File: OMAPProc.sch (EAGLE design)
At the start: 11 parts

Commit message: Pre-reinstall commit
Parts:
- removed C30, C31, C32, C33: 0.1uF, SparkFun:CAP0402-CAP
- removed JP11: MPCS6PH, stan:MPCS6PH
- removed R18: 4.7k, rcl:R-US_R0402
- removed R19, R20: 1.5k, rcl:R-US_R0402
- removed SHIFT1: TXS0108E, user:TXS0108E
- added C1, C15, C16, C17, C18, C19, C2, C21, C22, C3, C8: 0.1uF, biomimetic:CAP0402-CAP
- added C10, C11, C12, C13, C14, C4, C5, C6, C9: 1uF, biomimetic:CAP0402-CAP
- added C20: (no value), biomimetic:CAP0603-CAP
- added C7: 22uF, biomimetic:CAP0603-CAP
- added CAM2: ECAM50_5642_MOD, biomimetic:ECAM50_5642_MOD
- added IC1: MIC5335-SPYMT, biomimetic:MIC5335-SPYMT
- added IC2: MIC5335-MGYMT, biomimetic:MIC5335-MGYMT
- added IC3: TXS0108ERGY, biomimetic:TXS0108ERGY
- added JP1: Console, biomimetic:MOLEX_503480-0600
- added JP2: ImageProc, biomimetic:MOLEX_503480-0600
- added R1, R2: 1.5k, biomimetic:RESISTOR0402-RES
- added R3, R4, R5, R6, R7: 10k, biomimetic:RESISTOR0402-RES
- added R8: DNP, biomimetic:RESISTOR0402-RES
- added S1: SW_RESET, SparkFun-Electromechanical:SWITCH-MOMENTARY-2-SMD-1101NE
- added S2: SW_PWRON, SparkFun-Electromechanical:SWITCH-MOMENTARY-2-SMD-1101NE
- added SDCARD1: MICROSD, biomimetic:MICROSD
- CAM1: value AXK7L28227G(LI-VM01CM) -> LI-VM01CM; device user:AXK7L28227G(LI-VM01CM) -> biomimetic:LI-VM01CM
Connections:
- removed net N$18: SHIFT1.B1
- removed net N$22: SHIFT1.B2
- removed net N$27: SHIFT1.B3
- removed net N$30: SHIFT1.B4
- removed net N$31: SHIFT1.B5
- removed net N$33: SHIFT1.B6
- removed net N$34: SHIFT1.B7
- removed net N$35: SHIFT1.B8
- removed net OMAP_1.8V: C30.1, C32.1, CAM1.DOVDD(2.8V), CAM1.DVDD(1.8V), R18.2, R19.2, R20.2, SHIFT1.OE, SHIFT1.VCCA
- removed net OMAP_3.0V: C31.2, CAM1.AVDD(2.8V)
- removed net OMAP_3.3V: C33.1, SHIFT1.VCCB
- removed net OMAP_GND: C30.2, C31.1, C32.2, C33.2, CAM1.AGND, CAM1.DGND, JP11.2, R18.1, SHIFT1.GND
- removed net OMAP_SPI2_CLK: SHIFT1.A1
- removed net OMAP_SPI2_CS0: SHIFT1.A4
- removed net OMAP_SPI2_CS1: SHIFT1.A5
- removed net OMAP_SPI2_IRQ: SHIFT1.A6
- removed net OMAP_SPI2_SIMO: SHIFT1.A2
- removed net OMAP_SPI2_SOMI: SHIFT1.A3
- removed net OMAP_SPI4_CLK: SHIFT1.A7
- removed net OMAP_SPI4_SIMO: SHIFT1.A8
- removed net TERMINAL_CTS: JP11.6
- removed net TERMINAL_RTS: JP11.5
- removed net TERMINAL_RX: JP11.3
- removed net TERMINAL_TX: JP11.4
- new net !RESET: CAM1_S.!RESET, CAM2_S.!RESET, SOM1_CLOCKRESET.SYS_NRESWARM
- new net 1.8V: C1.2, C11.1, C15.1, C19.1, C2.1, C4.1, C5.2, CAM1_DOVDD.V+, CAM1_DVDD.V+, CAM2_DOVDD.V+, IC2.1.8V, IC3.OE, IC3.VCCA, R1.1, R2.1
- new net 2.8V: C10.1, C18.1, C3.1, C6.1, CAM1_AVDD.V+, CAM2_AVDD.V+, IC2.2.8V
- new net 3.0V: C14.1, IC1.3.0
- new net 3.3V: C13.1, C16.1, C17.1, CAM2_AFVCC.V+, IC1.3.3V, IC3.VCCB
- new net GND: C1.1, C10.2, C11.2, C12.1, C13.2, C14.2, C15.2, C16.2, C17.2, C18.2, C19.2, C2.2, C20.2, C21.2, C22.2, C3.2, C4.2, C5.1, C6.2, C7.2, C8.2, C9.1, CAM1_AGND.V-, CAM1_DGND.V-, CAM1_S.STANDBY, CAM2_AFVCC.V-, CAM2_AVDD.V-, CAM2_DOVDD.V-, CAM2_S.PWDN, IC1.GND, IC2.GND, IC3.GND, JP1.1, JP2.3, JP2.5, SDCARD1.CASE, SDCARD1.COM, SDCARD1.VSS, SOM1_DGND.V-
- new net MSTR_NRST: C21.1, S1.1, SOM1_CLOCKRESET.MSTR_NRST
- new net N$3: S1.2, S2.2
- new net PWRON: C22.1, S2.1, SOM1_CLOCKRESET.PWRON
- new net SD1_CD: R8.1, SDCARD1.CD, SOM1_GPIO.UP_GPIO_127
- new net SD1_CLK: SDCARD1.CLK, SOM1_SDMMC.SD1_CLK
- new net SD1_CMD: R3.1, SDCARD1.CMD, SOM1_SDMMC.SD1_CMD
- new net SD1_DATA0: R4.1, SDCARD1.DAT0, SOM1_SDMMC.SD1_DATA0
- new net SD1_DATA1: R5.1, SDCARD1.DAT1, SOM1_SDMMC.SD1_DATA1
- new net SD1_DATA2: R6.1, SDCARD1.DAT2, SOM1_SDMMC.SD1_DATA2
- new net SD1_DATA3: R7.1, SDCARD1.DAT3/CD, SOM1_SDMMC.SD1_DATA3
- new net UARTA_CTS: JP1.6, SOM1_UART.UP_UARTA_CTS
- new net UARTA_RTS: JP1.2, SOM1_UART.UP_UARTA_RTS
- new net UARTA_RX: JP1.4, SOM1_UART.UP_UARTA_RX
- new net UARTA_TX: JP1.5, SOM1_UART.UP_UARTA_TX
- new net UARTB_RX: IC3.A2, SOM1_UART.UP_UARTB_RX
- new net UARTB_RX_3V3: IC3.B2, JP2.4
- new net UARTB_TX: IC3.A1, SOM1_UART.UP_UARTB_TX
- new net UARTB_TX_3V3: IC3.B1, JP2.6
- new net VMMC1: C7.1, C8.1, R3.2, R4.2, R5.2, R6.2, R7.2, R8.2, SDCARD1.VDD, SOM1_SDMMC.VMMC1
- new net V_BATT: C12.2, C20.1, C9.2, IC1.EN_3.0V, IC1.EN_3.3V, IC1.VIN, IC2.EN_1.8V, IC2.EN_2.8V, IC2.VIN, JP2.1, JP2.2, SOM1_MAIN_BATTERY.V+
- net CAM_D0: now also CAM1_S.D0, CAM2_S.D2, SOM1_CSI.CSI_D0; no longer CAM1.D0
- net CAM_D1: now also CAM1_S.D1, CAM2_S.D3, SOM1_CSI.CSI_D1; no longer CAM1.D1
- net CAM_D2: now also CAM1_S.D2, CAM2_S.D4, SOM1_CSI.CSI_D2; no longer CAM1.D2
- net CAM_D3: now also CAM1_S.D3, CAM2_S.D5, SOM1_CSI.CSI_D3; no longer CAM1.D3
- net CAM_D4: now also CAM1_S.D4, CAM2_S.D6, SOM1_CSI.CSI_D4; no longer CAM1.D4
- net CAM_D5: now also CAM1_S.D5, CAM2_S.D7, SOM1_CSI.CSI_D5; no longer CAM1.D5
- net CAM_D6: now also CAM1_S.D6, CAM2_S.D8, SOM1_CSI.CSI_D6; no longer CAM1.D6
- net CAM_D7: now also CAM1_S.D7, CAM2_S.D9, SOM1_CSI.CSI_D7; no longer CAM1.D7
- net CAM_HSYNC: now also CAM1_S.HSYNC, CAM2_S.HREF, SOM1_CSI.CSI_HSYNC; no longer CAM1.HSYNC
- net CAM_MCLK: now also CAM1_S.MCLK, CAM2_S.XCLK, SOM1_CSI.CSI_XCLKA; no longer CAM1.MCLK
- net CAM_PCLK: now also CAM1_S.PCLK, CAM2_S.PCLK, SOM1_CSI.CSI_PCLK; no longer CAM1.PCLK
- net CAM_SCLK: now also CAM1_S.SCLK, CAM2_S.SCLK, R1.2, SOM1_I2C.UP_I2C2_SCL; no longer CAM1.SCLK, R20.1
- net CAM_SDATA: now also CAM1_S.SDATA, CAM2_S.SDATA, R2.2, SOM1_I2C.UP_I2C2_SDA; no longer CAM1.SDATA, R19.1
- net CAM_VSYNC: now also CAM1_S.VSYNC, CAM2_S.VSYNC, SOM1_CSI.CSI_VSYNC; no longer CAM1.VSYNC

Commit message: Near-final placement, partial route
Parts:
- removed C18, C19, C2: 0.1uF, biomimetic:CAP0402-CAP
- removed C4: 1uF, biomimetic:CAP0402-CAP
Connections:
- net 1.8V: no longer C19.1, C2.1, C4.1
- net 2.8V: no longer C18.1
- net GND: no longer C18.2, C19.2, C2.2, C4.2
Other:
- moved on the sheet: C1, C17, C3, C5, C6, CAM1_AGND, CAM1_AVDD, CAM1_DGND, CAM1_DOVDD, CAM1_DVDD, CAM2_AFVCC, CAM2_AVDD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

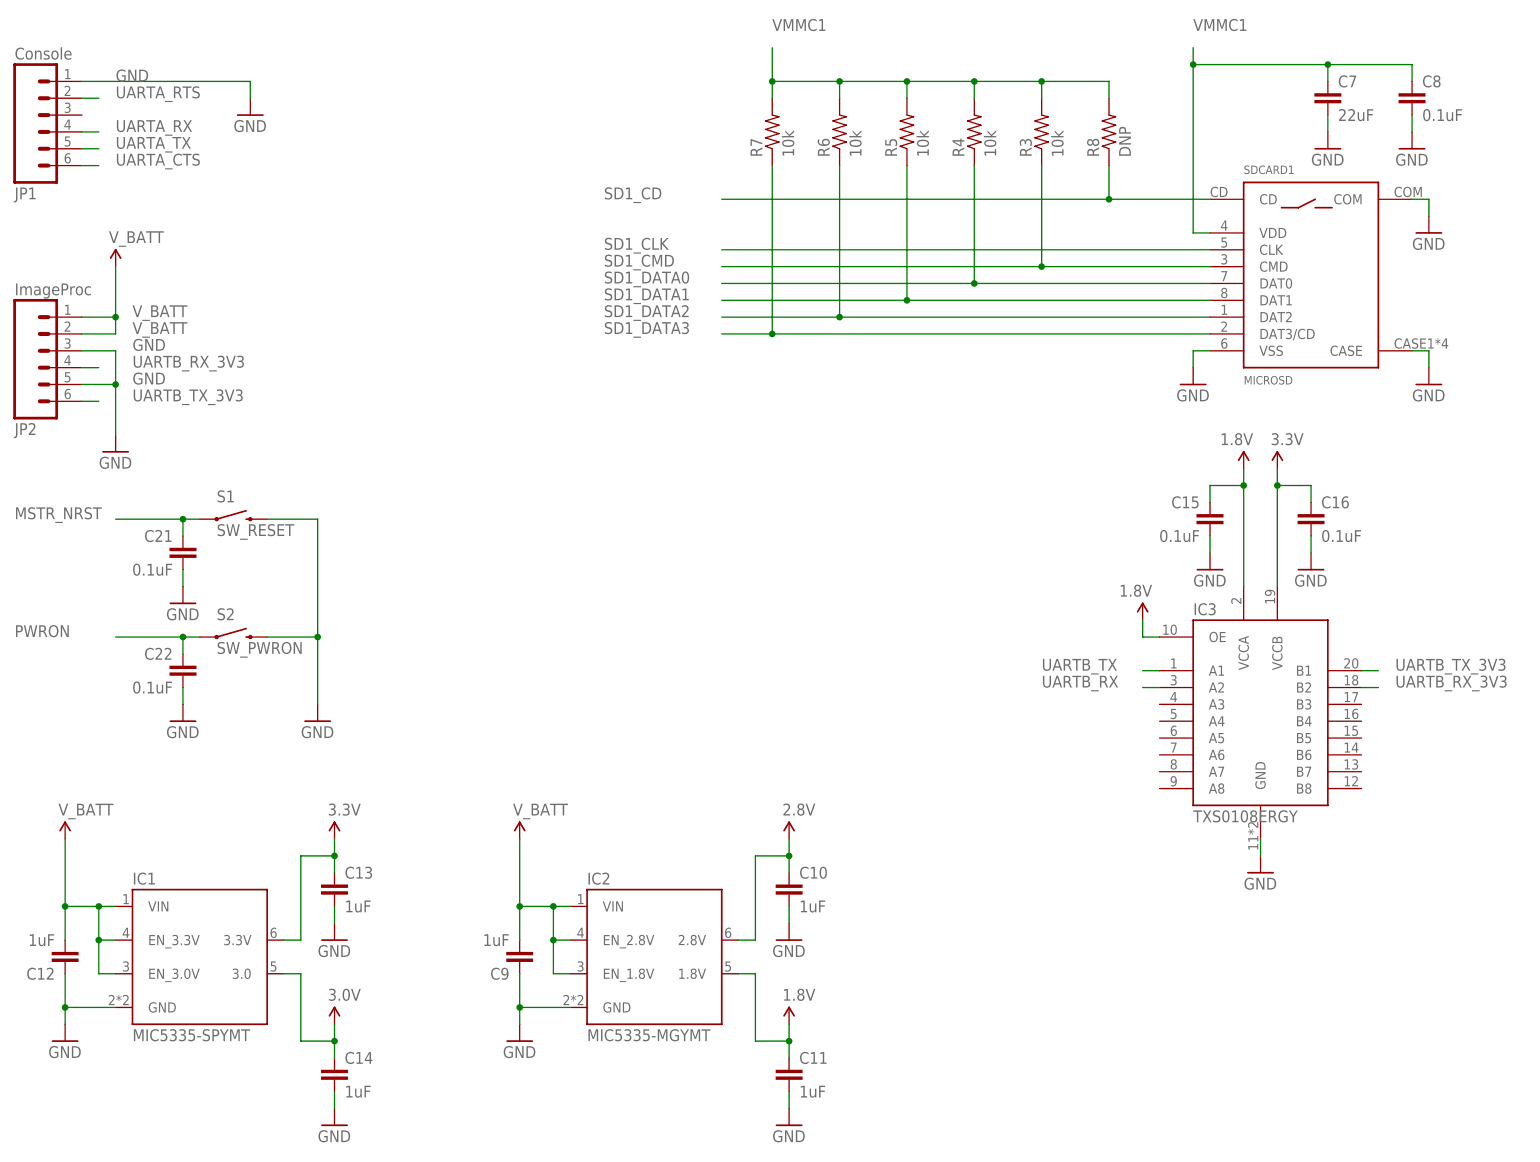
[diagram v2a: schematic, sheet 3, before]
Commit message: Routing and silkscreen complete.
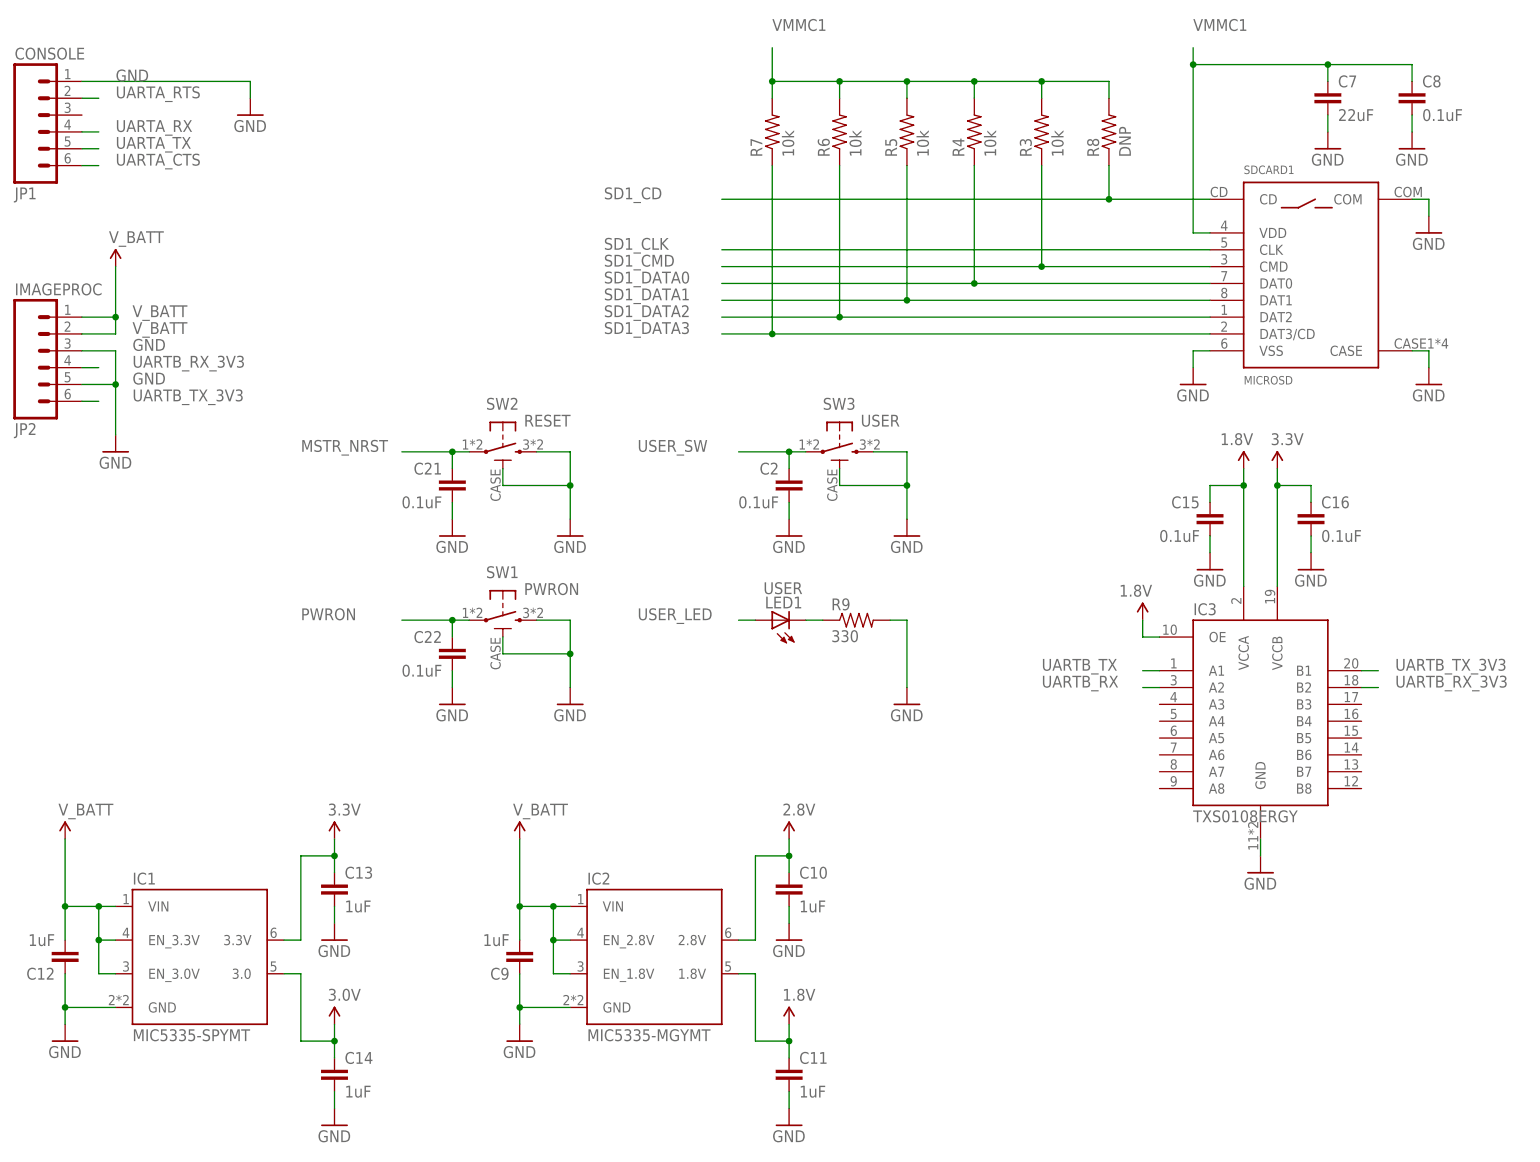
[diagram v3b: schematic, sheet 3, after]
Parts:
- removed S1: SW_RESET, SparkFun-Electromechanical:SWITCH-MOMENTARY-2-SMD-1101NE
- removed S2: SW_PWRON, SparkFun-Electromechanical:SWITCH-MOMENTARY-2-SMD-1101NE
- added C2: 0.1uF, biomimetic:CAP0402-CAP
- added LED1: USER, biomimetic:LED0603
- added R9: 330, biomimetic:RESISTOR0402-RES
- added SW1: PWRON, biomimetic:KMR421GLFS
- added SW2: RESET, biomimetic:KMR421GLFS
- added SW3: USER, biomimetic:KMR421GLFS
- C20: value (none) -> 22uF
- JP1: value Console -> CONSOLE
- JP2: value ImageProc -> IMAGEPROC
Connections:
- new net N$1: SOM1_BACKUP_BATT.V+
- new net N$2: SOM1VIO_1V8.V+
- new net USER_LED: LED1.A, SOM1_GPIO.UP_GPIO_129
- new net USER_SW: C2.1, SOM1_GPIO.UP_GPIO_128, SW3.P
- net GND: now also C2.2, R9.2, SW1.CASE, SW1.S, SW2.CASE, SW2.S, SW3.CASE, SW3.S
- net MSTR_NRST: now also SW2.P; no longer S1.1
- net N$3: now also LED1.C, R9.1; no longer S1.2, S2.2
- net PWRON: now also SW1.P; no longer S2.1
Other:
- moved on the sheet: C21, C22
